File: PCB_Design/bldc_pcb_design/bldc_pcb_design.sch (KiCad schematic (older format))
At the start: 34 parts, among them IC1 DRV8305NPHPR, U1 ESP32-WROOM-32U, U2 BSC022N04LS6ATMA1, U3 BSC022N04LS6ATMA1, U4 BSC022N04LS6ATMA1, U5 BSC022N04LS6ATMA1, U6 BSC022N04LS6ATMA1, U7 BSC022N04LS6ATMA1

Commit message: Started schematics design from scratch
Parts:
- removed R3, R4: 10K, symbol Device:R
- removed R5: R, symbol Device:R
- removed U1: ESP32-WROOM-32U, RF_Module:ESP32-WROOM-32U, symbol RF_Module:ESP32-WROOM-32U
- added C?: 10 uF 50V, symbol Device:C_Small
- added C?: 0.1 uF 50V, symbol Device:C_Small
- added C?: 1 uF 50V, symbol Device:C_Small
- added J?: Conn_01x04_Female, symbol Connector:Conn_01x04_Female
- added R? (x2): 10k, symbol Device:R_Small_US
- added SW?: BOOT, symbol Switch:SW_Push
- added SW?: RESET, symbol Switch:SW_Push
- added U?: ESP32-WROOM-32D, RF_Module:ESP32-WROOM-32, symbol RF_Module:ESP32-WROOM-32D
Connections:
- net labels added: 3V3_IN, 3V3_ISOLATED, 3V3_REGULATED, BOOT, RESET, RX, TX
- net labels removed: CAN_RX, CAN_TX, CLK, CMD, ESP_BOOT, ESP_EN, EXT_ENC_nCS, FET_TEMP, I2C_CLK, I2C_DATA, IO2, IO4, ITN_ENC_nCS, MOTOR_TEMP, RXD0, SCK, SCS, SD0, SD1, SD2, SD3, SDI, SDO, SHD, SPI_SCLK, SWP, TXD0
- wire segments 203 -> 195
- no-connect marks 2 -> 1
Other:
- note added: "3V3_ISOLATED is used to \npower ESP32 when board \nisn't being powered \nby VIN."
- note added: "Decoupling caps, \nkeep close to\npower pins\n"
- note added: "Don't connect 3V3_ISOLATED \nwhile board is powered by Battery"
- note added: "Microcontroller (ESP32)"
- note removed: "BLDC Actuator \n"
- note removed: "BLDC Controller"
- note removed: "ESP32 Rf Module"
- moved on the sheet: C1, C10, C2, C3, C4, C5, C6, C7, C8, C9, IC1, R1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

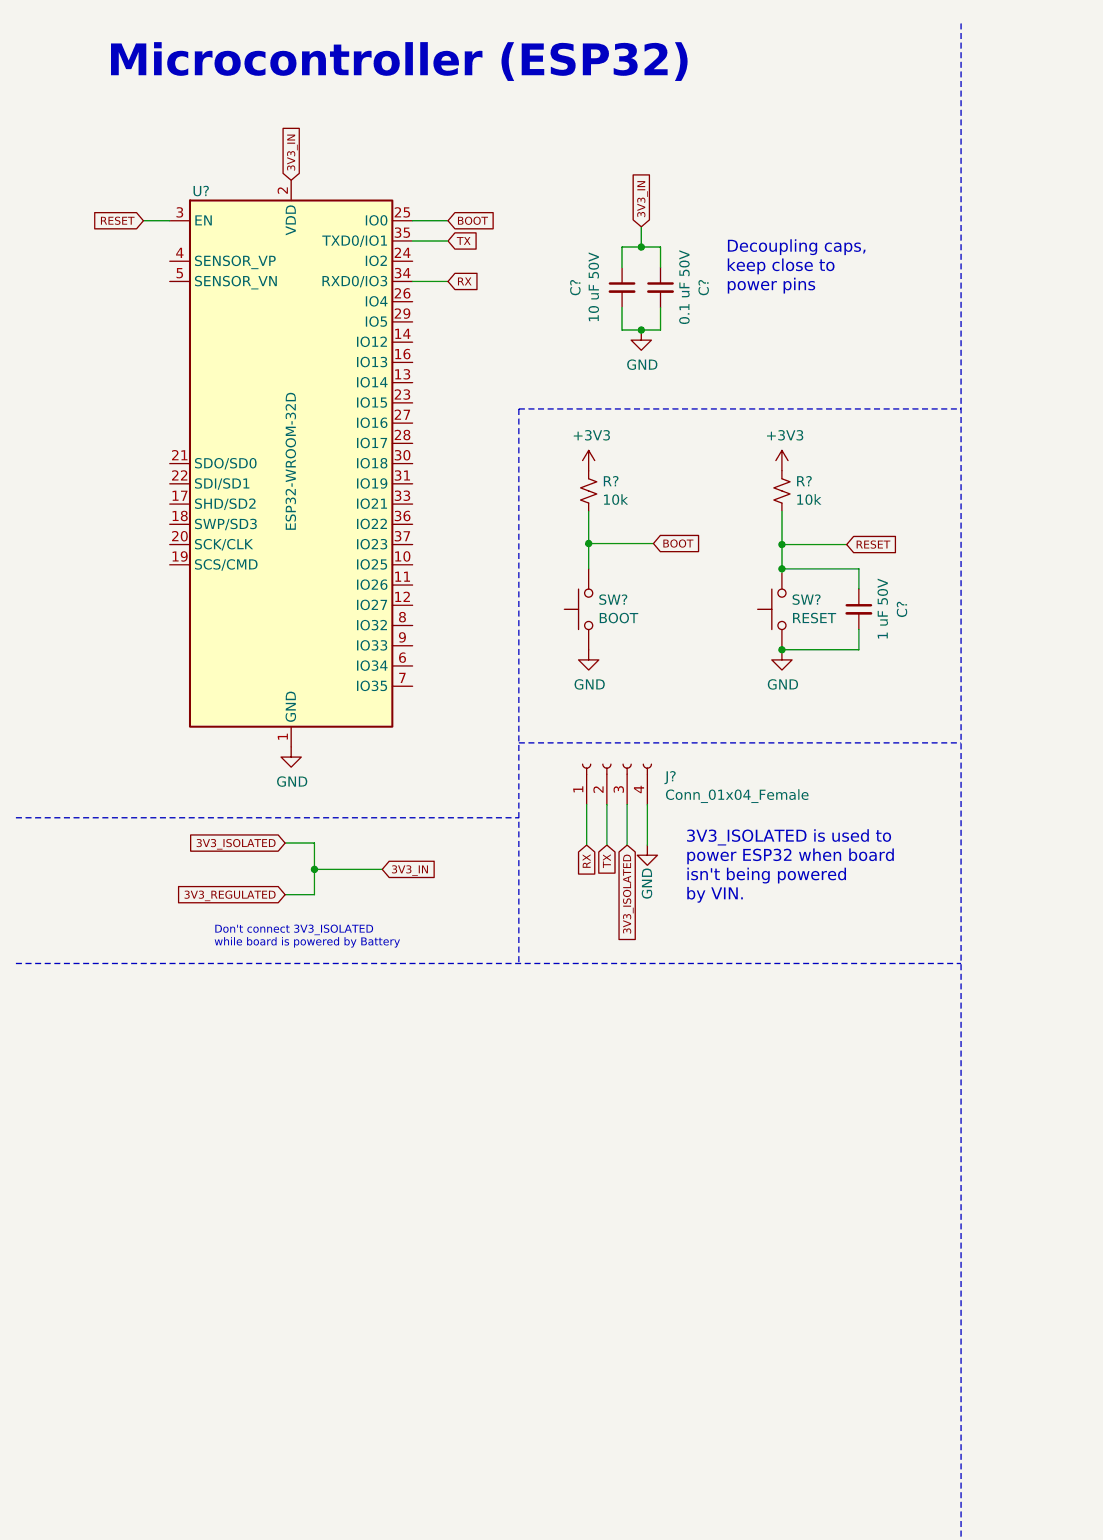
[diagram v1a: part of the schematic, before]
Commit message: Completed schematics of ESP32 and Encoder
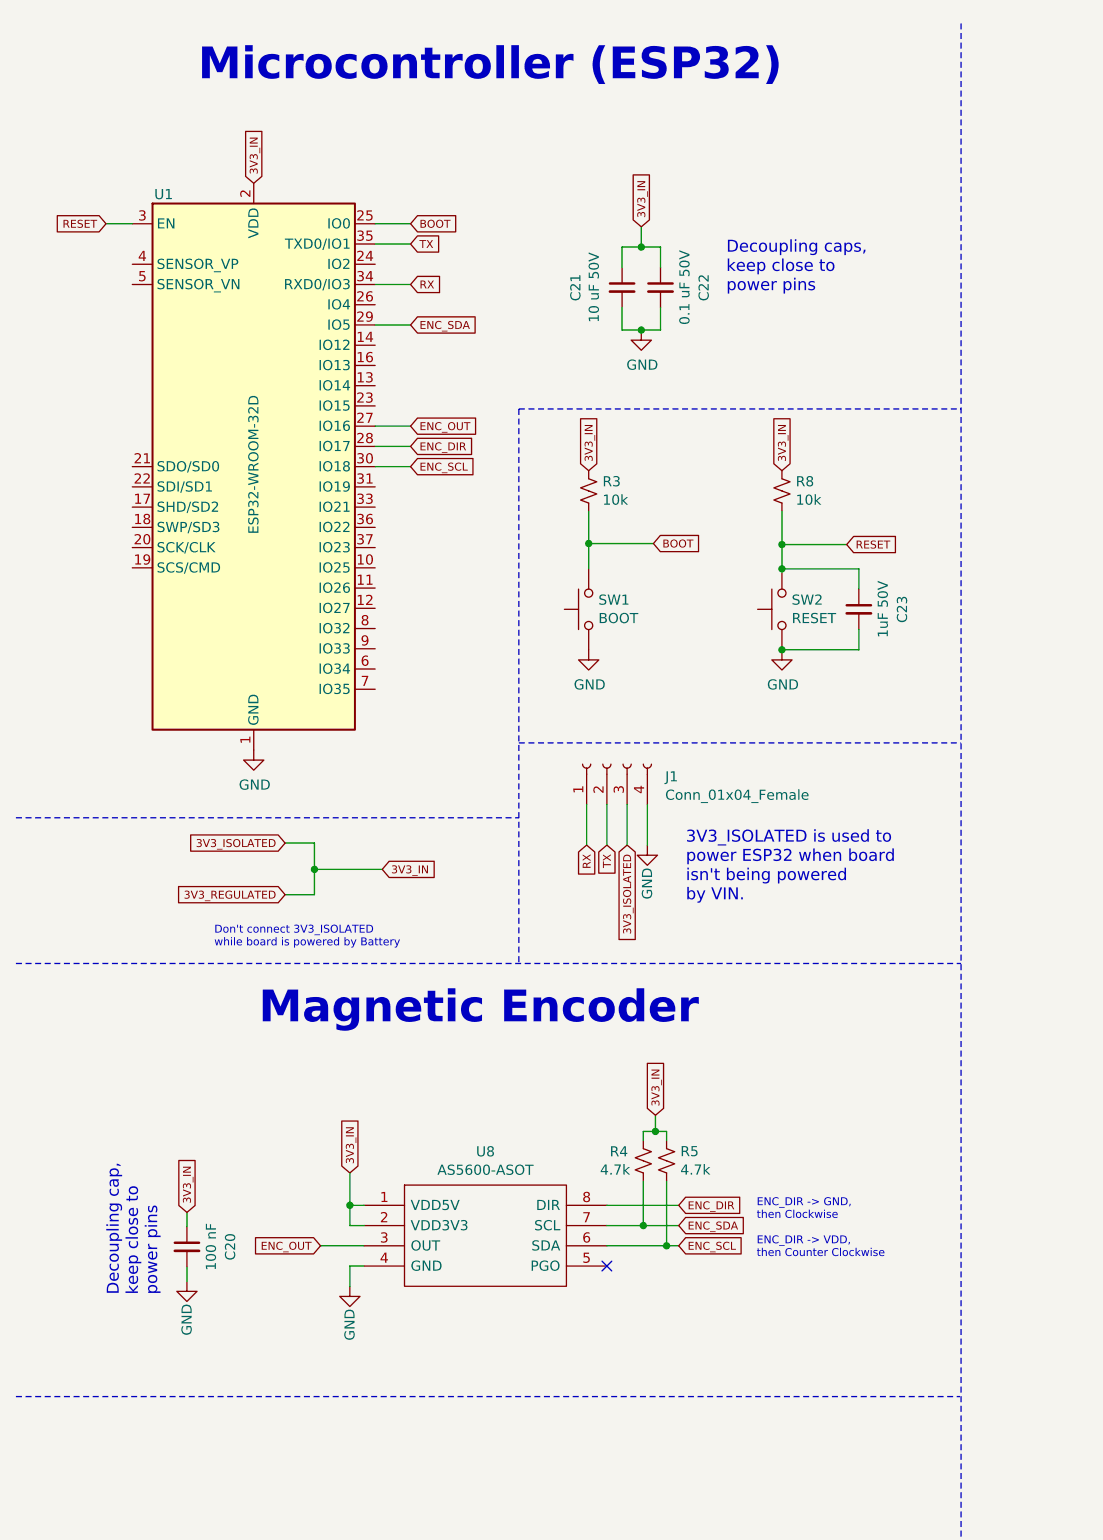
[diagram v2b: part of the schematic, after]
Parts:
- added C20: 100 nF, symbol Device:C_Small
- added R4, R5: 4.7k, symbol Device:R_Small_US
- added U8: AS5600-ASOT, SOIC127P600X175-8N, symbol AS5600-ASOT:AS5600-ASOT
- C23: renamed from C?; value 1 uF 50V -> 1uF 50V
- gave numbers to parts that had none: 8
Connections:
- net labels added: ENC_DIR, ENC_OUT, ENC_SCL, ENC_SDA
- wire segments 195 -> 220
- no-connect marks 1 -> 2
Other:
- note added: "Decoupling cap,\nkeep close to\npower pins\n"
- note added: "ENC_DIR -> GND, \nthen Clockwise\n\nENC_DIR -> VDD, \nthen Counter Clockwise"
- note added: "Magnetic Encoder"
- moved on the sheet: U1

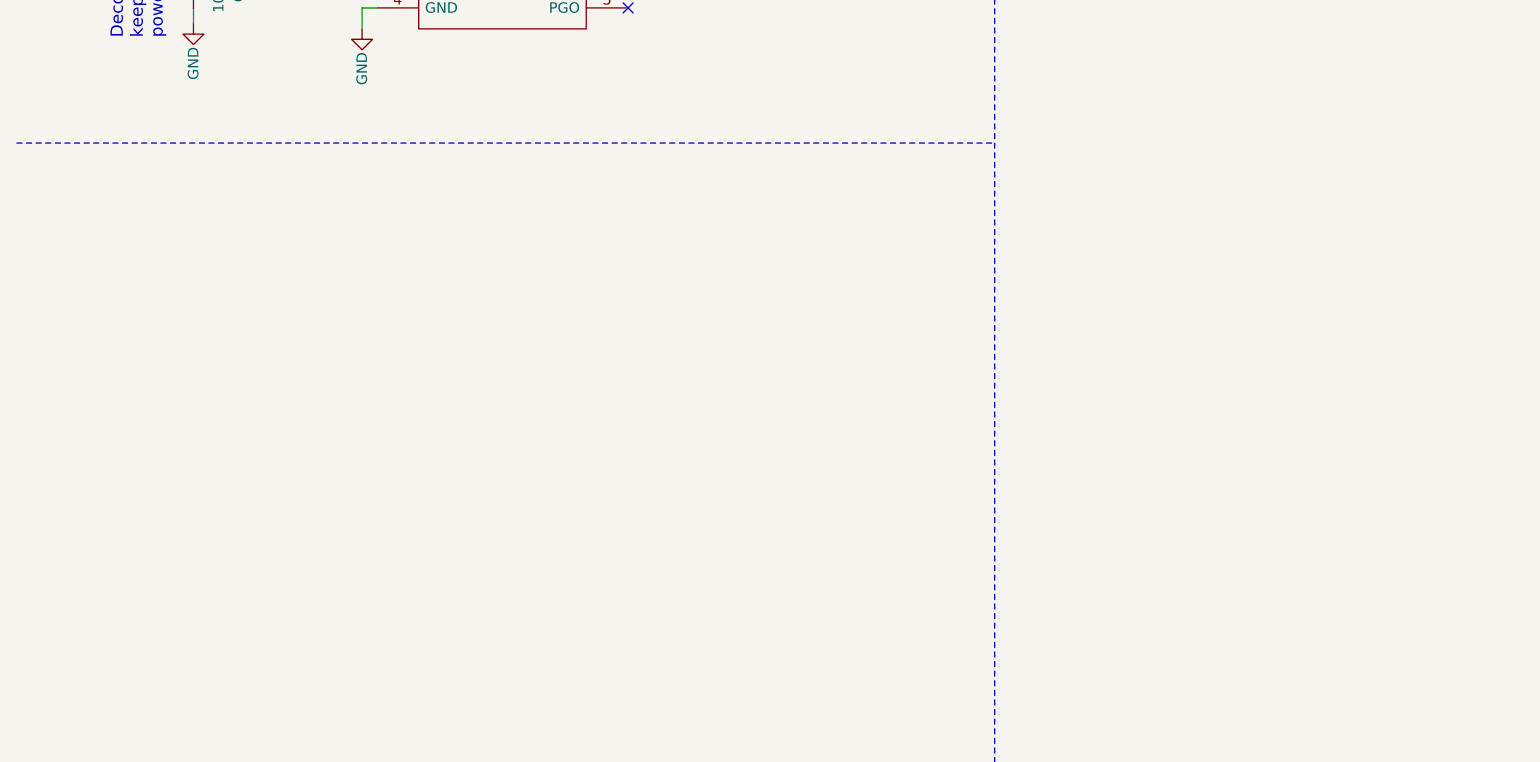
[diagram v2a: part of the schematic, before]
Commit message: WIP: Added Switching mode regulator schematics
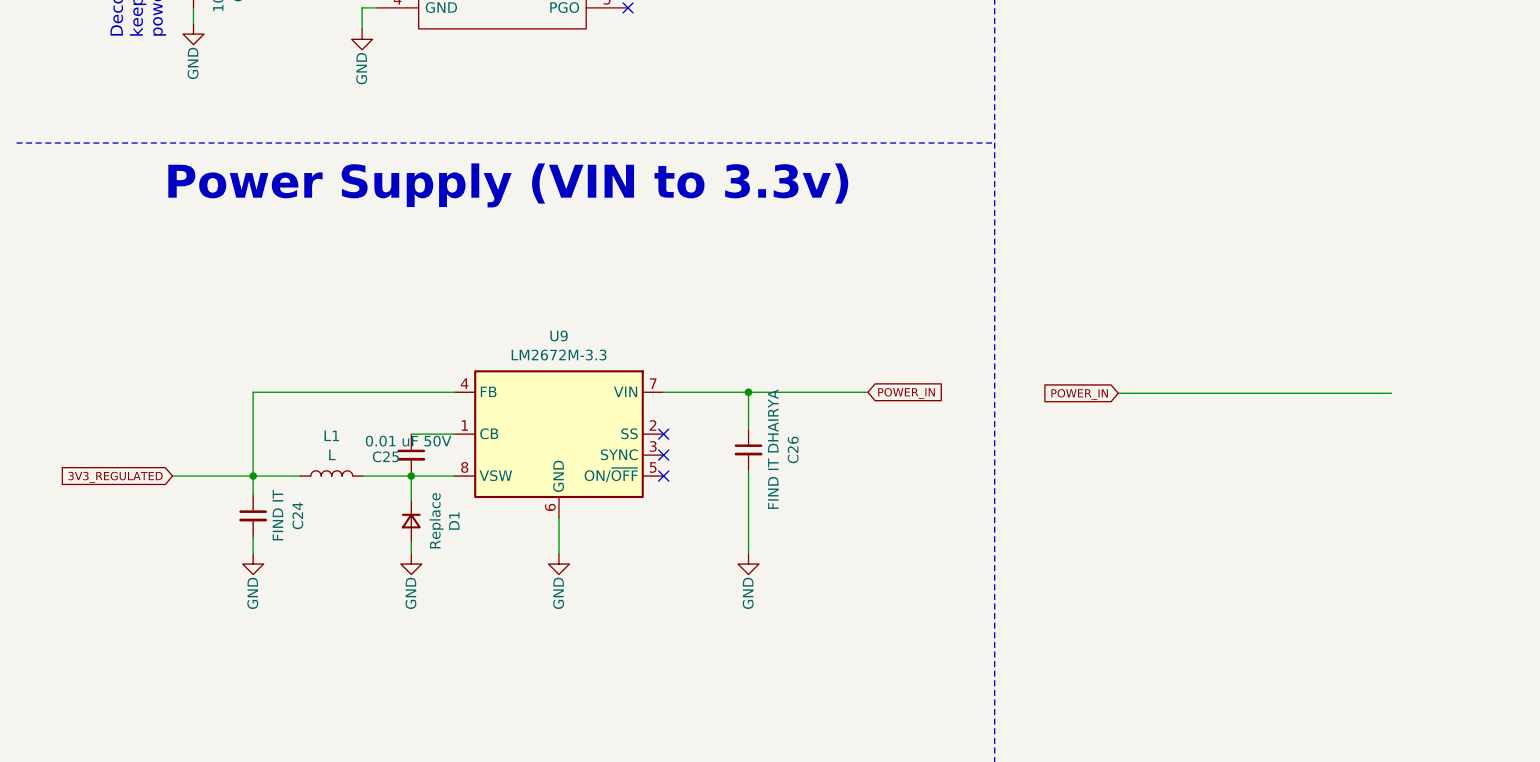
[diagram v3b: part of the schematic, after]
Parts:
- added C24: FIND IT, symbol Device:C_Small
- added C25: 0.01 uF 50V, symbol Device:C_Small
- added C26: FIND IT DHAIRYA, symbol Device:C_Small
- added D1: Replace, symbol Device:D_Small
- added L1: L, symbol Device:L
- added U9: LM2672M-3.3, Package_SO:SOIC-8_3.9x4.9mm_P1.27mm, symbol Regulator_Switching:LM2672M-3.3
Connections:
- net labels added: POWER_IN
- wire segments 220 -> 237
- no-connect marks 2 -> 5
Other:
- note added: "Power Supply (VIN to 3.3v)"
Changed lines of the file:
@@
 Wire Wire Line
 	2435 2595 2260 2595
+$Comp
+L Regulator_Switching:LM2672M-3.3 U9
+U 1 1 6131BA8C
+P 3075 8680
+F 0 "U9" H 3075 9147 50  0000 C CNN
+F 1 "LM2672M-3.3" H 3075 9056 50  0000 C CNN
+F 2 "Package_SO:SOIC-8_3.9x4.9mm_P1.27mm" H 3125 8330 50  0001 L CIN
+F 3 "http://www.ti.com/lit/ds/symlink/lm2672.pdf" H 3075 8680 50  0001 C CNN
+	1    3075 8680
+	-1   0    0    -1
+$EndComp
+Text Notes 1190 7580 0    157  ~ 31
+Power Supply (VIN to 3.3v)
+$Comp
+L power:GND #PWR021
+U 1 1 61396B76
+P 3075 9250
+F 0 "#PWR021" H 3075 9000 50  0001 C CNN
+F 1 "GND" V 3075 9060 50  0000 C CNN
+F 2 "" H 3075 9250 50  0001 C CNN
+F 3 "" H 3075 9250 50  0001 C CNN
+	1    3075 9250
+	1    0    0    -1
+$EndComp
+NoConn ~ 3575 8880
+NoConn ~ 3575 8680
+NoConn ~ 3575 8780
+Wire Wire Line
+	3575 8480 3980 8480
+Text GLabel 4550 8480 2    39   Input ~ 0
+POWER_IN
+Text GLabel 5745 8485 0    39   Input ~ 0
+POWER_IN
+Wire Wire Line
+	5745 8485 7050 8485
+$Comp
+L Device:C_Small C26
+U 1 1 614136E9
+P 3980 8755
+F 0 "C26" V 4195 8755 50  0000 C CNN
+F 1 "FIND IT DHAIRYA" V 4100 8755 50  0000 C CNN
+F 2 "" H 3980 8755 50  0001 C CNN
+F 3 "~" H 3980 8755 50  0001 C CNN
+	1    3980 8755
+	1    0    0    -1
+$EndComp
+Wire Wire Line
+	3980 8655 3980 8480
+$Comp
+L power:GND #PWR022
+U 1 1 61425A4E
+P 3980 9250
+F 0 "#PWR022" H 3980 9000 50  0001 C CNN
+F 1 "GND" V 3980 9060 50  0000 C CNN
+F 2 "" H 3980 9250 50  0001 C CNN
+F 3 "" H 3980 9250 50  0001 C CNN
+	1    3980 9250
+	1    0    0    -1
+$EndComp
+$Comp
+L Device:C_Small C25
+U 1 1 6143826A
+P 2370 8780
+F 0 "C25" H 2250 8770 50  0000 C CNN
+F 1 "0.01 uF 50V" H 2355 8845 50  0000 C CNN
+F 2 "" H 2370 8780 50  0001 C CNN
+F 3 "~" H 2370 8780 50  0001 C CNN
+	1    2370 8780
+	1    0    0    -1
+$EndComp
+$Comp
+L Device:C_Small C24
+U 1 1 6143855F
+P 1615 9070
+F 0 "C24" V 1830 9070 50  0000 C CNN
+F 1 "FIND IT" V 1735 9070 50  0000 C CNN
+F 2 "" H 1615 9070 50  0001 C CNN
+F 3 "~" H 1615 9070 50  0001 C CNN
+	1    1615 9070
+	1    0    0    -1
+$EndComp
+$Comp
+L Device:D_Small D1
+U 1 1 6143D556
+P 2370 9095
+F 0 "D1" H 2370 9302 50  0000 C CNN
+F 1 "Replace" H 2370 9211 50  0000 C CNN
+F 2 "" V 2370 9095 50  0001 C CNN
+F 3 "~" V 2370 9095 50  0001 C CNN
+	1    2370 9095
+	0    1    1    0
+$EndComp
+Text GLabel 1230 8880 0    39   Input ~ 0
+3V3_REGULATED
+Wire Wire Line
+	3980 8855 3980 9250
+Wire Wire Line
+	3075 9080 3075 9250
+$Comp
+L power:GND #PWR019
+U 1 1 614ACA2E
+P 1615 9250
+F 0 "#PWR019" H 1615 9000 50  0001 C CNN
+F 1 "GND" V 1615 9060 50  0000 C CNN
+F 2 "" H 1615 9250 50  0001 C CNN
+F 3 "" H 1615 9250 50  0001 C CNN
+	1    1615 9250
+	1    0    0    -1
+$EndComp
+Wire Wire Line
+	1615 9170 1615 9250
+Wire Wire Line
+	1615 8970 1615 8880
+Wire Wire Line
+	3980 8480 4550 8480
+Connection ~ 3980 8480
+Wire Wire Line
+	1230 8880 1615 8880
+Connection ~ 1615 8880
+Wire Wire Line
+	1615 8880 1840 8880
+Connection ~ 2370 8880
+Wire Wire Line
+	2370 8880 2575 8880
+Wire Wire Line
+	2370 8680 2575 8680
+$Comp
+L power:GND #PWR020
+U 1 1 61562ED3
+P 2370 9250
+F 0 "#PWR020" H 2370 9000 50  0001 C CNN
+F 1 "GND" V 2370 9060 50  0000 C CNN
+F 2 "" H 2370 9250 50  0001 C CNN
+F 3 "" H 2370 9250 50  0001 C CNN
+	1    2370 9250
+	1    0    0    -1
+$EndComp
+Wire Wire Line
+	2370 8995 2370 8880
+Wire Wire Line
+	2370 9195 2370 9250
+$Comp
+L Device:L L1
+U 1 1 61466B3D
+P 1990 8880
+F 0 "L1" V 2180 8880 50  0000 C CNN
+F 1 "L" V 2089 8880 50  0000 C CNN
+F 2 "" H 1990 8880 50  0001 C CNN
+F 3 "~" H 1990 8880 50  0001 C CNN
+	1    1990 8880
+	0    -1   -1   0
+$EndComp
+Wire Wire Line
+	2140 8880 2370 8880
+Wire Wire Line
+	2575 8480 1615 8480
+Wire Wire Line
+	1615 8480 1615 8880
 $EndSCHEMATC
